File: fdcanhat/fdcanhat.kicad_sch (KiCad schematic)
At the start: 0 parts

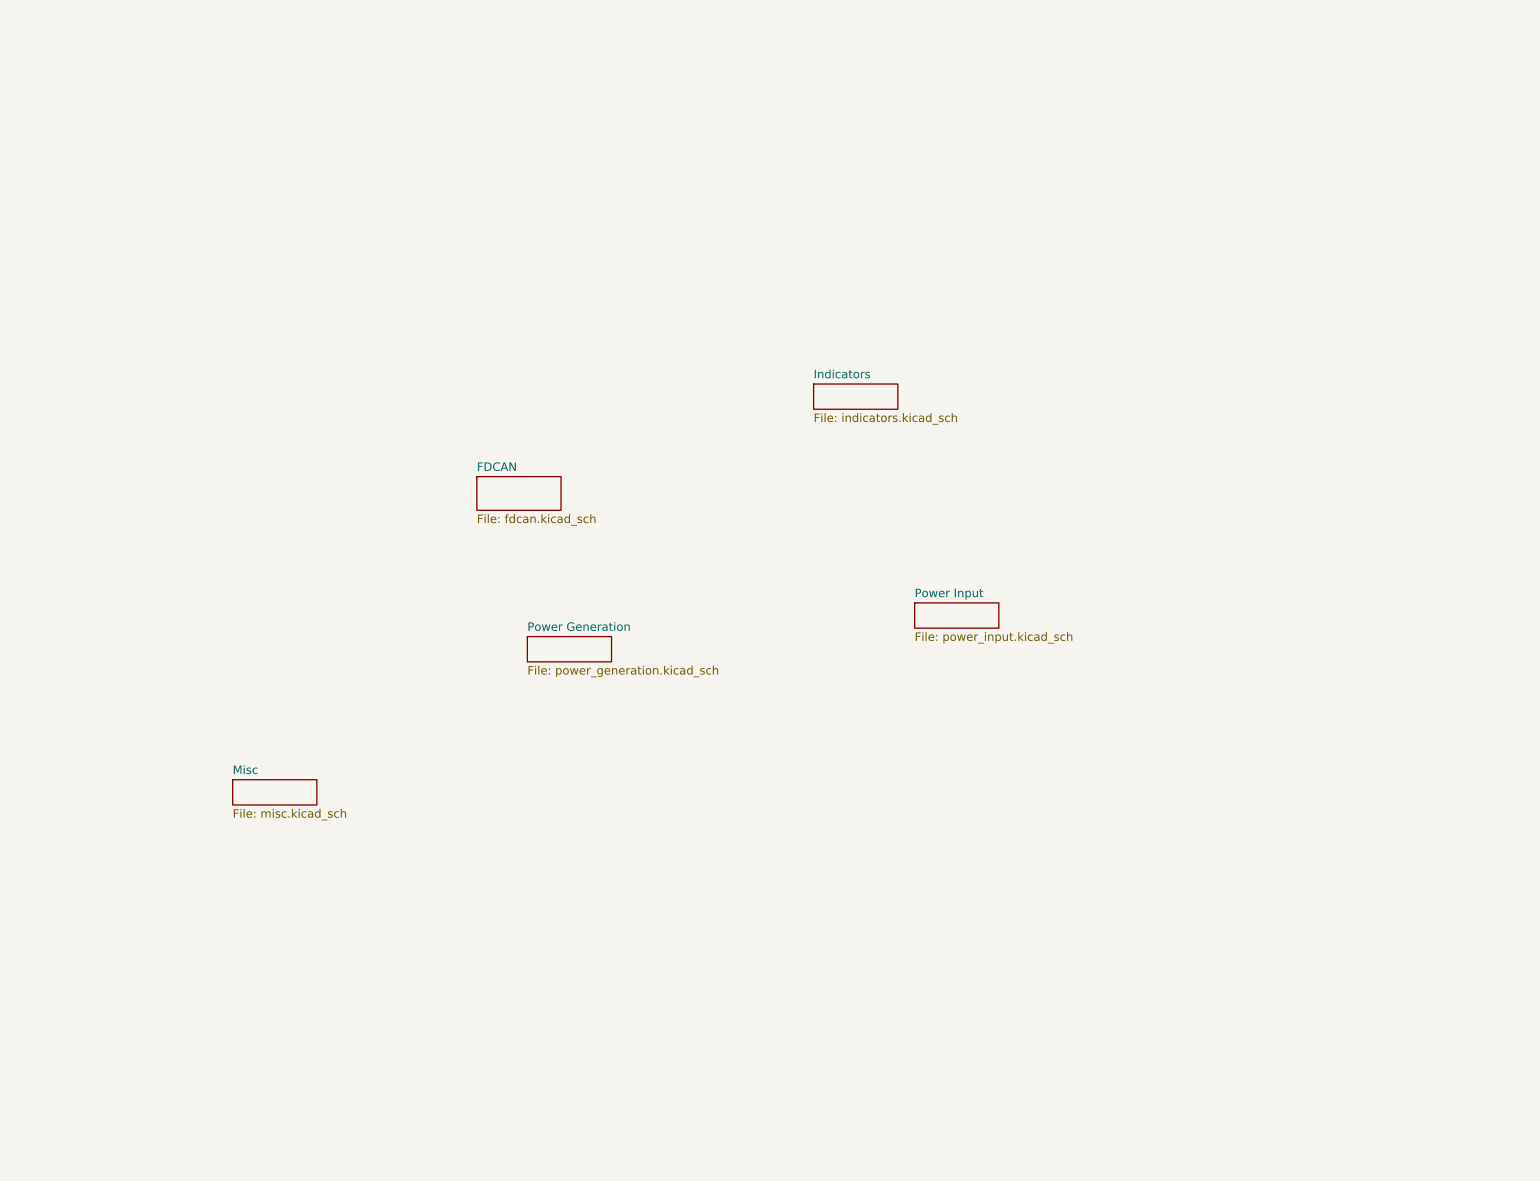
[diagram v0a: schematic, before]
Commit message: ish done with schematics
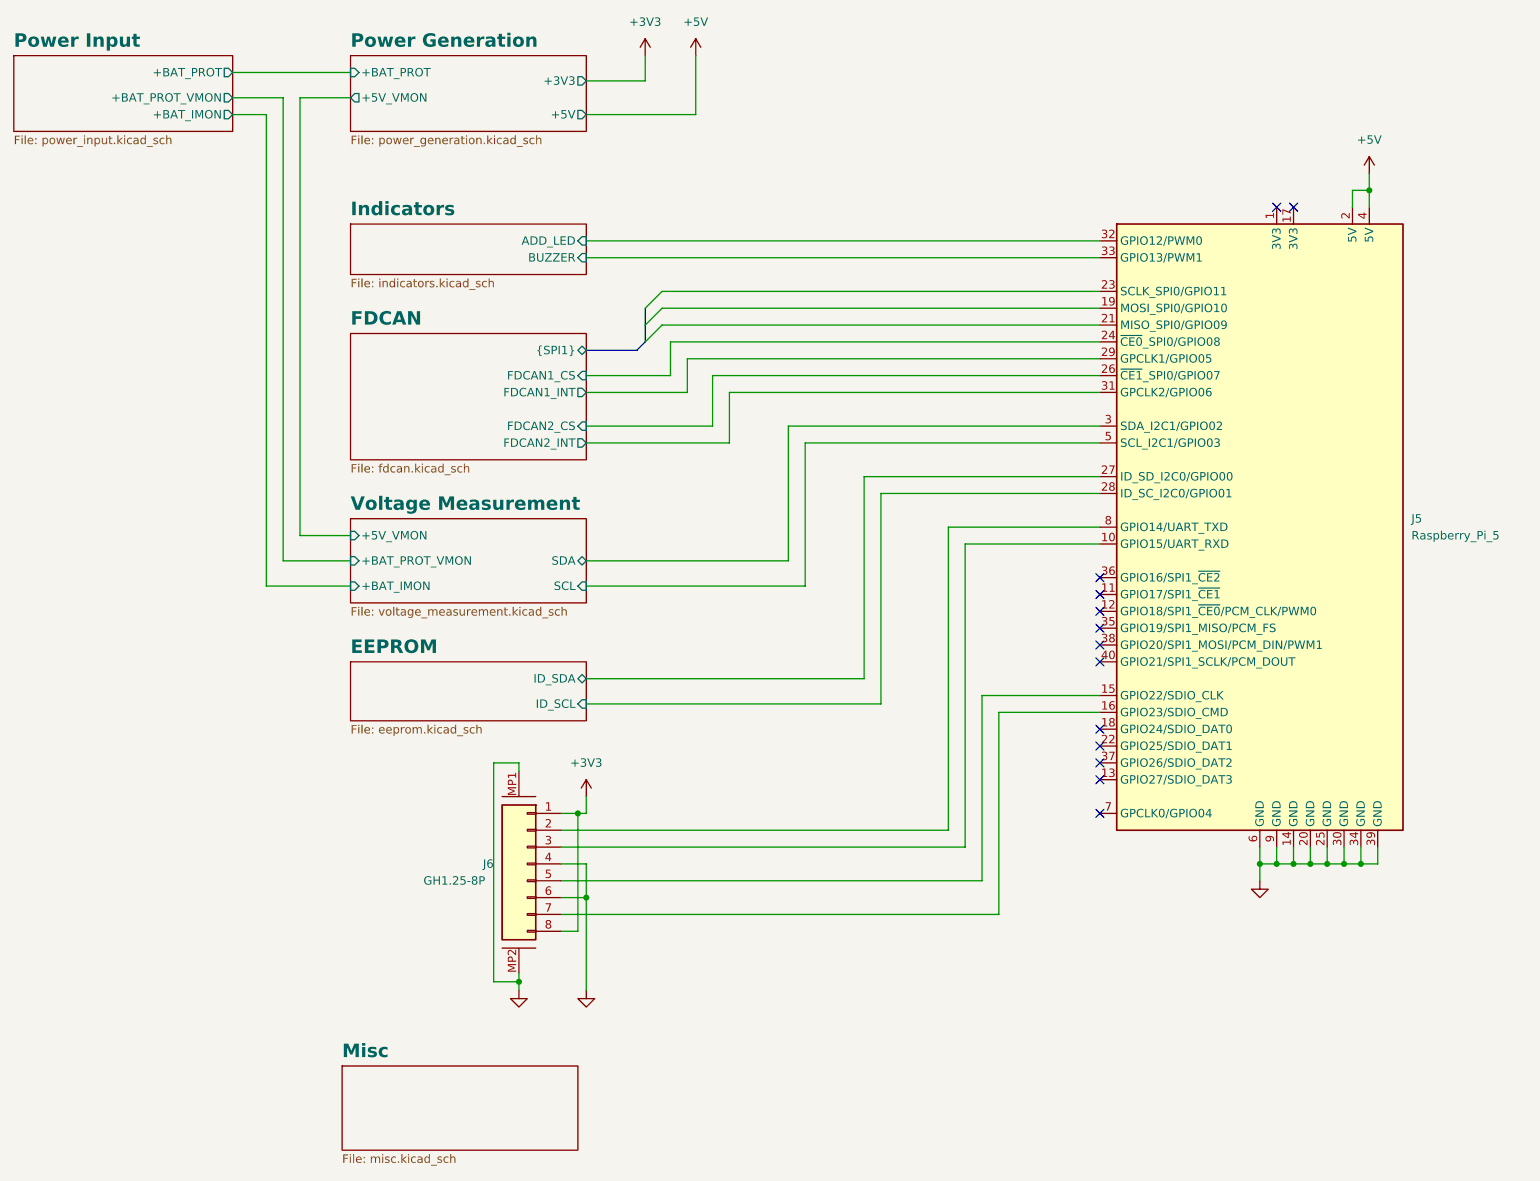
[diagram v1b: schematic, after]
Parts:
- added J5: Raspberry_Pi_5, symbol 0_connectors:Raspberry_Pi_5
- added J6: GH1.25-8P, symbol 0_connectors:Conn_01x08_Mounting
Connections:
- new net: J5.10 (GPIO15/UART_RXD), J6.3 (Pin_3)
- new net: J5.15 (GPIO22/SDIO_CLK), J6.5 (Pin_5)
- new net: J5.16 (GPIO23/SDIO_CMD), J6.7 (Pin_7)
- new net: J5.8 (GPIO14/UART_TXD), J6.2 (Pin_2)
- new net +3V3: J6.1 (Pin_1), J6.8 (Pin_8)
- new net +5V: J5.2 (5V), J5.4 (5V)
- new net EEPROM/ID_SCL: J5.28 (ID_SC_I2C0/GPIO01)
- new net EEPROM/ID_SDA: J5.27 (ID_SD_I2C0/GPIO00)
- new net FDCAN/FDCAN1_CS: J5.24 (~{CE0}_SPI0/GPIO08)
- new net FDCAN/FDCAN1_INT: J5.29 (GPCLK1/GPIO05)
- new net FDCAN/FDCAN2_CS: J5.26 (~{CE1}_SPI0/GPIO07)
- new net FDCAN/FDCAN2_INT: J5.31 (GPCLK2/GPIO06)
- new net GND: J5.14 (GND), J5.20 (GND), J5.25 (GND), J5.30 (GND), J5.34 (GND), J5.39 (GND), J5.6 (GND), J5.9 (GND), J6.4 (Pin_4), J6.6 (Pin_6), J6.MP1, J6.MP2
- new net Indicators/ADD_LED: J5.32 (GPIO12/PWM0)
- new net Indicators/BUZZER: J5.33 (GPIO13/PWM1)
- new net Voltage Measurement/SCL: J5.5 (SCL_I2C1/GPIO03)
- new net Voltage Measurement/SDA: J5.3 (SDA_I2C1/GPIO02)
- no-connect marks 0 -> 13
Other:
- added sheet EEPROM (eeprom.kicad_sch)
- added sheet Voltage Measurement (voltage_measurement.kicad_sch)
- sheet FDCAN ports: added FDCAN1_CS, FDCAN1_INT, FDCAN2_CS, FDCAN2_INT, {SPI1}; removed none
- sheet Indicators ports: added ADD_LED, BUZZER; removed none
- sheet Power Generation ports: added +3V3, +5V, +5V_VMON, +BAT_PROT; removed none
- sheet Power Input ports: added +BAT_IMON, +BAT_PROT, +BAT_PROT_VMON; removed none

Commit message: board layout done, ready for routing
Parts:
- J1: renamed from J5; footprint (none) -> 0_connectors:PinHeader_2x20_P2.54mm_Vertical; now left out of the parts list
- J2: renamed from J6; footprint (none) -> 0_connectors:SM08B-GHS-TB-LF-SN; LCSC (none) -> C265111
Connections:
- net RTK_RXD: now reaches J1.10 (GPIO15/UART_RXD), J2.3 (Pin_3)
- net RTK_PPS: now reaches J1.15 (GPIO22/SDIO_CLK), J2.5 (Pin_5)
- net RTK_EVENT: now reaches J1.16 (GPIO23/SDIO_CMD), J2.7 (Pin_7)
- net SPI0_MOSI: now reaches J1.19 (MOSI_SPI0/GPIO10)
- net SPI0_MISO: now reaches J1.21 (MISO_SPI0/GPIO09)
- net SPI0_SCK: now reaches J1.23 (SCLK_SPI0/GPIO11)
- net RTK_TXD: now reaches J1.8 (GPIO14/UART_TXD), J2.2 (Pin_2)
- net EEPROM/ID_SCL: no longer names the net of J1.28 (ID_SC_I2C0/GPIO01)
- net EEPROM/ID_SDA: no longer names the net of J1.27 (ID_SD_I2C0/GPIO00)
- net FDCAN/FDCAN1_CS renamed FDCAN1_CS
- net FDCAN/FDCAN1_INT renamed FDCAN1_INT
- net FDCAN/FDCAN2_CS renamed FDCAN2_CS
- net FDCAN/FDCAN2_INT renamed FDCAN2_INT
- net Indicators/ADD_LED renamed ADD_LED
- net Indicators/BUZZER renamed BUZZER
- net Voltage Measurement/SCL renamed MON_SCL
- net Voltage Measurement/SDA renamed MON_SDA
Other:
- removed sheet EEPROM
- sheet FDCAN ports: added {SPI0}; removed {SPI1}
- sheet Voltage Measurement ports: added MON_SCL, MON_SDA; removed SCL, SDA

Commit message: almost done
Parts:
- removed J2: GH1.25-8P, 0_connectors:SM08B-GHS-TB-LF-SN, symbol 0_connectors:Conn_01x08_Mounting
- added J2: GH1.25-5P, 0_connectors:SM05B-GHS-TB-LF-SN, symbol 0_connectors:Conn_01x05_Mounting
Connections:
- net +3V3: now also J2.5 (Pin_5)
- net ADD_LED: now also J1.37 (GPIO26/SDIO_DAT2); no longer J1.32 (GPIO12/PWM0)
- net GND: now also J2.1 (Pin_1), J2.MP1, J2.MP2
- net RTK_PPS: now also J1.7 (GPCLK0/GPIO04), J2.2 (Pin_2); no longer J1.15 (GPIO22/SDIO_CLK)
- net RTK_RXD: now also J2.3 (Pin_3)
- net RTK_TXD: now also J2.4 (Pin_4)
- net BUZZER: no longer names the net of J1.33 (GPIO13/PWM1)
- net RTK_EVENT: no longer names the net of J1.16 (GPIO23/SDIO_CMD)
- no-connect marks 13 -> 15
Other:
- sheet Indicators ports: added none; removed BUZZER

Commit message: done doublechecking, going for review
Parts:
- J2: LCSC (none) -> C189896
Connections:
- no-connect marks 15 -> 17
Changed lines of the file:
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@@
+	)
+	(no_connect
+		(at 200.66 124.46)
 	)
 	(no_connect
@@
 	(no_connect
 		(at 200.66 111.76)
+	)
+	(no_connect
+		(at 200.66 121.92)
 	)
 	(no_connect
@@
 		(dnp no)
 		(fields_autoplaced yes)
-		(property "Reference" "#PWR07"
+		(property "Reference" "#PWR06"
 			(at 120.65 151.13 0)
 			(effects
@@
 			(project "fdcanhat"
 				(path "/4375c315-c696-43df-ab5b-868bd3f1287b"
-					(reference "#PWR07")
+					(reference "#PWR06")
 					(unit 1)
 				)
@@
 		(dnp no)
 		(fields_autoplaced yes)
-		(property "Reference" "#PWR06"
+		(property "Reference" "#PWR04"
 			(at 121.92 128.27 0)
 			(effects
@@
 			(project "fdcanhat"
 				(path "/4375c315-c696-43df-ab5b-868bd3f1287b"
-					(reference "#PWR06")
+					(reference "#PWR04")
 					(unit 1)
 				)
@@
 			)
 		)
+		(property "LCSC" "C189896"
+			(at 114.3 130.81 0)
+			(effects
+				(font
+					(size 1.27 1.27)
+				)
+				(hide yes)
+			)
+		)
 		(pin "1"
 		)
@@
 		(dnp no)
 		(fields_autoplaced yes)
-		(property "Reference" "#PWR04"
+		(property "Reference" "#PWR05"
 			(at 113.03 151.13 0)
 			(effects
@@
 			(project "fdcanhat"
 				(path "/4375c315-c696-43df-ab5b-868bd3f1287b"
-					(reference "#PWR04")
+					(reference "#PWR05")
 					(unit 1)
 				)
@@
 		(dnp no)
 		(fields_autoplaced yes)
-		(property "Reference" "#PWR05"
+		(property "Reference" "#PWR07"
 			(at 224.79 156.21 0)
 			(effects
@@
 			(project "fdcanhat"
 				(path "/4375c315-c696-43df-ab5b-868bd3f1287b"
-					(reference "#PWR05")
+					(reference "#PWR07")
 					(unit 1)
 				)

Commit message: sent to production
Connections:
- net ADD_LED: now also J1.38 (GPIO20/SPI1_MOSI); no longer J1.37 (GPIO26/SDIO_DAT2)
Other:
- title: (none) -> Main
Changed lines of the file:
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@@
 	(paper "A4")
 	(title_block
+		(title "Main")
 		(date "2026-01-07")
 		(rev "1.0")
@@
 	)
 	(no_connect
-		(at 200.66 114.3)
-	)
-	(no_connect
 		(at 229.87 48.26)
 	)
 	(no_connect
+		(at 200.66 134.62)
+	)
+	(no_connect
